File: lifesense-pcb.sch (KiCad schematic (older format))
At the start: 2 parts

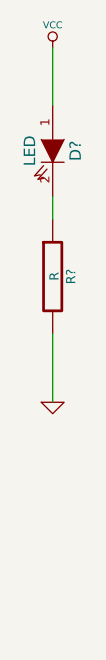
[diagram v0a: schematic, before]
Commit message: added resistor
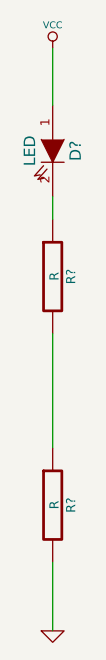
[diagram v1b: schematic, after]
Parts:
- added R?: R, symbol R
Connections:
- net GND: now also R?.2; no longer R?.2
- new net: R?.1, R?.2
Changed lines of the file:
@@
 LIBS:contrib
 LIBS:valves
+LIBS:lifesense-pcb-cache
 EELAYER 24 0
 EELAYER END
@@
 $EndComp
 Wire Wire Line
-	4150 2850 4150 3150
+	4150 3850 4150 4150
 $Comp
 L GND #PWR?
 U 1 1 5389F8DA
-P 4150 3150
-F 0 "#PWR?" H 4150 3150 30  0001 C CNN
-F 1 "GND" H 4150 3080 30  0001 C CNN
-F 2 "" H 4150 3150 60  0000 C CNN
-F 3 "" H 4150 3150 60  0000 C CNN
-	1    4150 3150
+P 4150 4150
+F 0 "#PWR?" H 4150 4150 30  0001 C CNN
+F 1 "GND" H 4150 4080 30  0001 C CNN
+F 2 "" H 4150 4150 60  0000 C CNN
+F 3 "" H 4150 4150 60  0000 C CNN
+	1    4150 4150
 	1    0    0    -1
 $EndComp
@@
 Wire Wire Line
 	4150 2350 4150 2250
+$Comp
+L R R?
+U 1 1 5389FBAE
+P 4150 3600
+F 0 "R?" V 4230 3600 40  0000 C CNN
+F 1 "R" V 4157 3601 40  0000 C CNN
+F 2 "" V 4080 3600 30  0000 C CNN
+F 3 "" H 4150 3600 30  0000 C CNN
+	1    4150 3600
+	1    0    0    -1
+$EndComp
+Wire Wire Line
+	4150 2850 4150 3350
 $EndSCHEMATC
